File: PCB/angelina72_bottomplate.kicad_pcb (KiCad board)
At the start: 2 copper layers, 176.4 x 111.6 mm, 9 parts

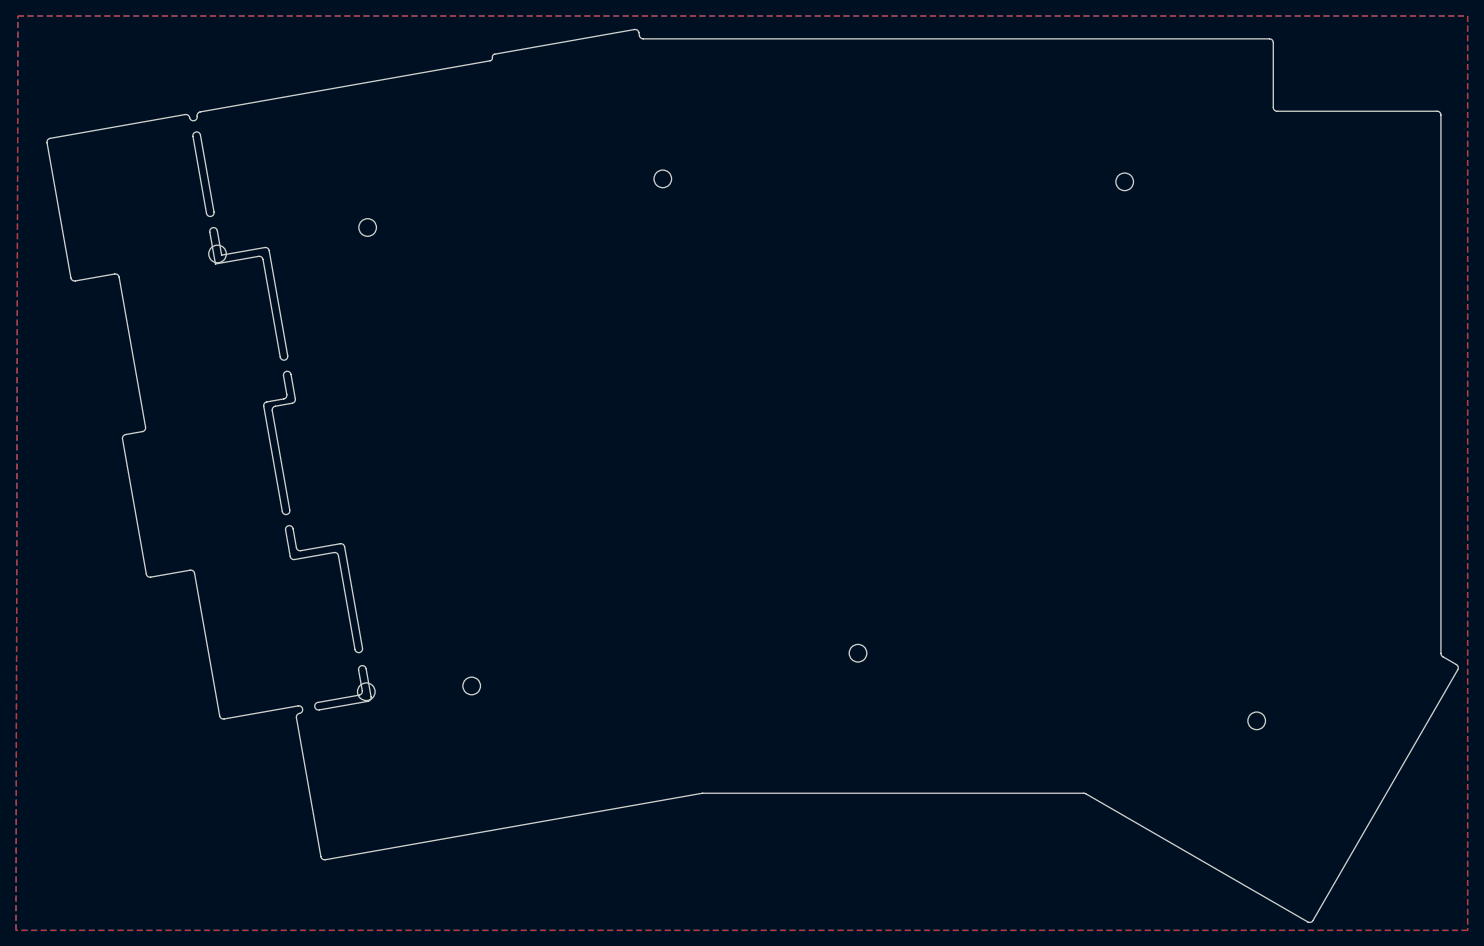
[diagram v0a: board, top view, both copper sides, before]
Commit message: Fix PCB, top plate, bottom plate
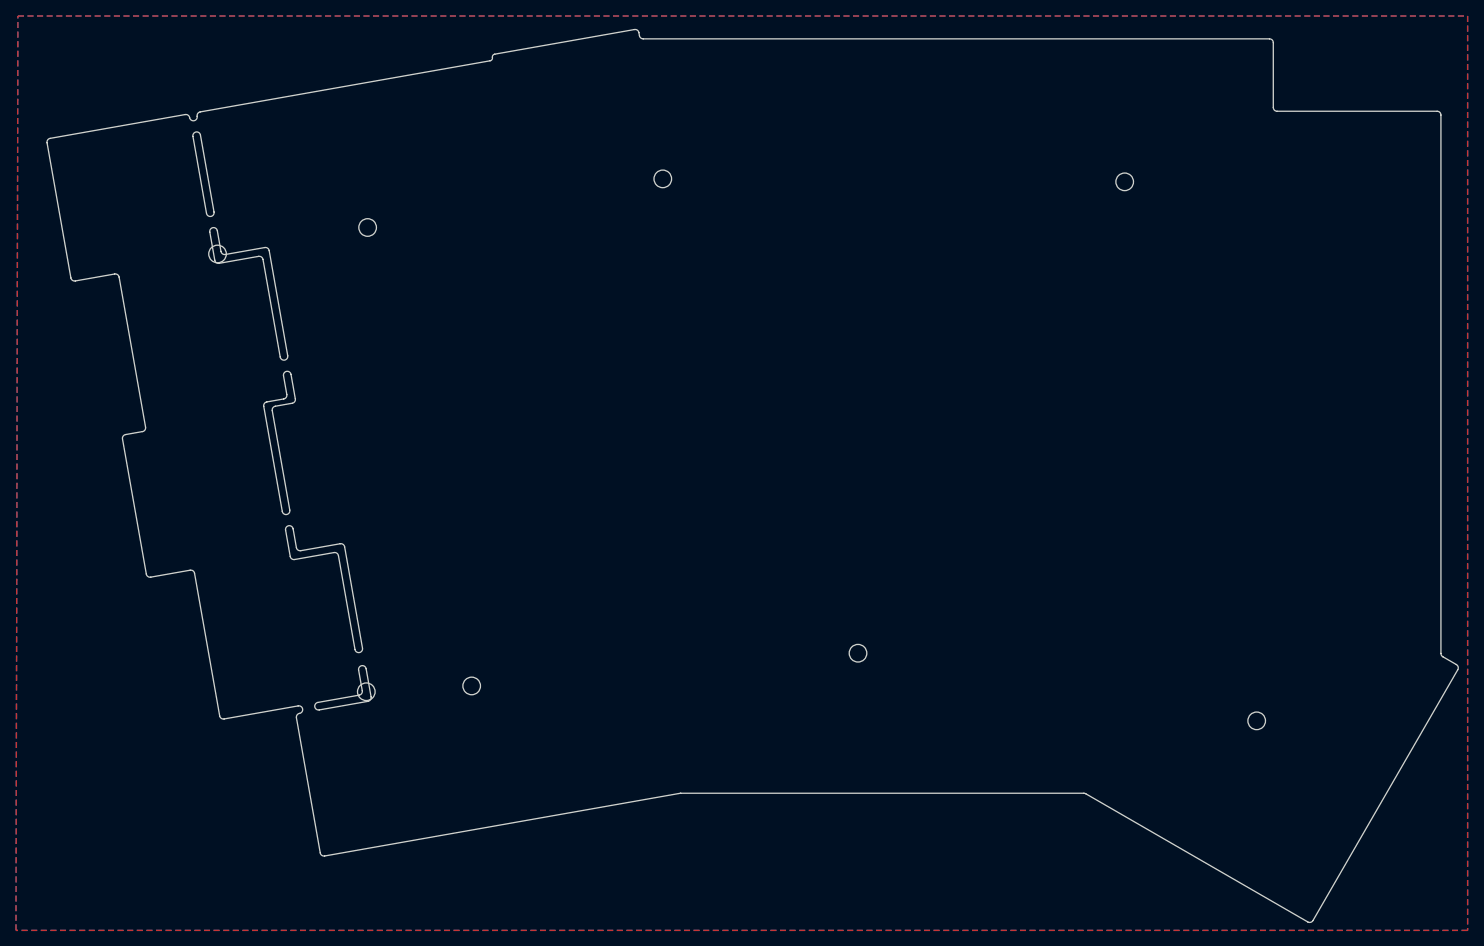
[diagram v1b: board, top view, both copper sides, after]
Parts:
- added REF**: Outline_MXCherry_1.25u, angelina72:Outline_MXCherry_1.25u, F.Cu at (148.9, 122.5)
- added REF**: Outline_MXCherry_1u, angelina72:Outline_MXCherry_1u, F.Cu at (74.3, 90.8)
- added REF**: Outline_MXCherry_1u, angelina72:Outline_MXCherry_1u, F.Cu at (55.2, 74.8)
- added REF**: Outline_MXCherry_1u, angelina72:Outline_MXCherry_1u, F.Cu at (74.0, 71.5)
- added REF**: Outline_MXCherry_1u, angelina72:Outline_MXCherry_1u, F.Cu at (92.8, 68.2)
- added REF**: Outline_MXCherry_1u, angelina72:Outline_MXCherry_1u, F.Cu at (102.2, 46.5)
- added REF**: Outline_MXCherry_1u, angelina72:Outline_MXCherry_1u, F.Cu at (83.6, 50.5)
- added REF**: Outline_MXCherry_1u, angelina72:Outline_MXCherry_1u, F.Cu at (64.8, 53.8)
- added REF**: Outline_MXCherry_1u, angelina72:Outline_MXCherry_1u, F.Cu at (46.1, 57.1)
- added REF**: Outline_MXCherry_1u, angelina72:Outline_MXCherry_1u, F.Cu at (173.9, 126.0)
- added REF**: Outline_MXCherry_1u, angelina72:Outline_MXCherry_1u, F.Cu at (190.4, 135.5)
- added REF**: Outline_MXCherry_1.25u, angelina72:Outline_MXCherry_1.25u, F.Cu at (125.1, 122.5)
- added REF**: Outline_MXCherry_1u, angelina72:Outline_MXCherry_1u, F.Cu at (199.9, 119.0)
- added REF**: Outline_MXCherry_1u, angelina72:Outline_MXCherry_1u, F.Cu at (160.8, 103.4)
- added REF**: Outline_MXCherry_1u, angelina72:Outline_MXCherry_1u, F.Cu at (179.9, 103.4)
- added REF**: Outline_MXCherry_1u, angelina72:Outline_MXCherry_1u, F.Cu at (122.7, 103.4)
- added REF**: Outline_MXCherry_1u, angelina72:Outline_MXCherry_1u, F.Cu at (141.8, 103.4)
- added REF**: Outline_MXCherry_1u, angelina72:Outline_MXCherry_1u, F.Cu at (170.4, 84.4)
- added REF**: Outline_MXCherry_1u, angelina72:Outline_MXCherry_1u, F.Cu at (132.3, 84.4)
- added REF**: Outline_MXCherry_1u, angelina72:Outline_MXCherry_1u, F.Cu at (113.2, 84.4)
- added REF**: Outline_MXCherry_1u, angelina72:Outline_MXCherry_1u, F.Cu at (151.3, 84.4)
- added REF**: Outline_MXCherry_1u, angelina72:Outline_MXCherry_1u, F.Cu at (170.4, 65.3)
- added REF**: Outline_MXCherry_1u, angelina72:Outline_MXCherry_1u, F.Cu at (100.8, 124.8)
- added REF**: Outline_MXCherry_1u, angelina72:Outline_MXCherry_1u, F.Cu at (151.3, 65.3)
- added REF**: Outline_MXCherry_1u, angelina72:Outline_MXCherry_1u, F.Cu at (113.2, 65.3)
- added REF**: Outline_MXCherry_1u, angelina72:Outline_MXCherry_1u, F.Cu at (132.3, 65.3)
- added REF**: Outline_MXCherry_1u, angelina72:Outline_MXCherry_1u, F.Cu at (122.7, 46.3)
- added REF**: Outline_MXCherry_1u, angelina72:Outline_MXCherry_1u, F.Cu at (141.8, 46.3)
- added REF**: Outline_MXCherry_1u, angelina72:Outline_MXCherry_1u, F.Cu at (160.8, 46.3)
- added REF**: Outline_MXCherry_1u, angelina72:Outline_MXCherry_1u, F.Cu at (179.9, 46.3)
- added REF**: Outline_MXCherry_1.25u, angelina72:Outline_MXCherry_1.25u, F.Cu at (79.7, 128.5)
- added REF**: Outline_MXCherry_1u, angelina72:Outline_MXCherry_1u, F.Cu at (102.2, 105.2)
- added REF**: Outline_MXCherry_1u, angelina72:Outline_MXCherry_1u, F.Cu at (64.7, 111.8)
- added REF**: Outline_MXCherry_1u, angelina72:Outline_MXCherry_1u, F.Cu at (83.4, 108.5)
- added REF**: Outline_MXCherry_1u, angelina72:Outline_MXCherry_1u, F.Cu at (93.0, 87.5)
- added REF**: Outline_MXCherry_1u, angelina72:Outline_MXCherry_1u, F.Cu at (55.5, 94.1)
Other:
- outline, holes or cut-outs redrawn

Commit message: Update PCBs
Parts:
- added REF**: Layout_Outline_PromicroBase, angelina72:Layout_Outline_PromicroBase, F.Cu at (113.2, 113.0)
- added REF**: Layout_Outline, angelina72:Layout_Outline, F.Cu at (113.2, 113.0)
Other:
- outline, holes or cut-outs redrawn
